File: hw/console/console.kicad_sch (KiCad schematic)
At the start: 147 parts, among them J1 Batt, J301 USB-C 16P, J401 microSD push-push, J501 SPK 8R, J601 FFC-40 0.5mm, Q601 N-MOSFET, SW1 Движок, SW101 UP, SW102 DOWN, SW103 LEFT, SW104 RIGHT, SW105 SELECT, SW106 START, SW107 A, SW108 B, SW109 C, SW110 D, SW2 RESET, SW301 FEL, U1 F133-A, U2 SY8089AAAC, U3 SY8089AAAC, U4 SY8089AAAC, U401 W25Q32JVSSIQ, U5 TP4056, U501 PAM8301, Y1 24 МГц, Y2 32.768 кГц

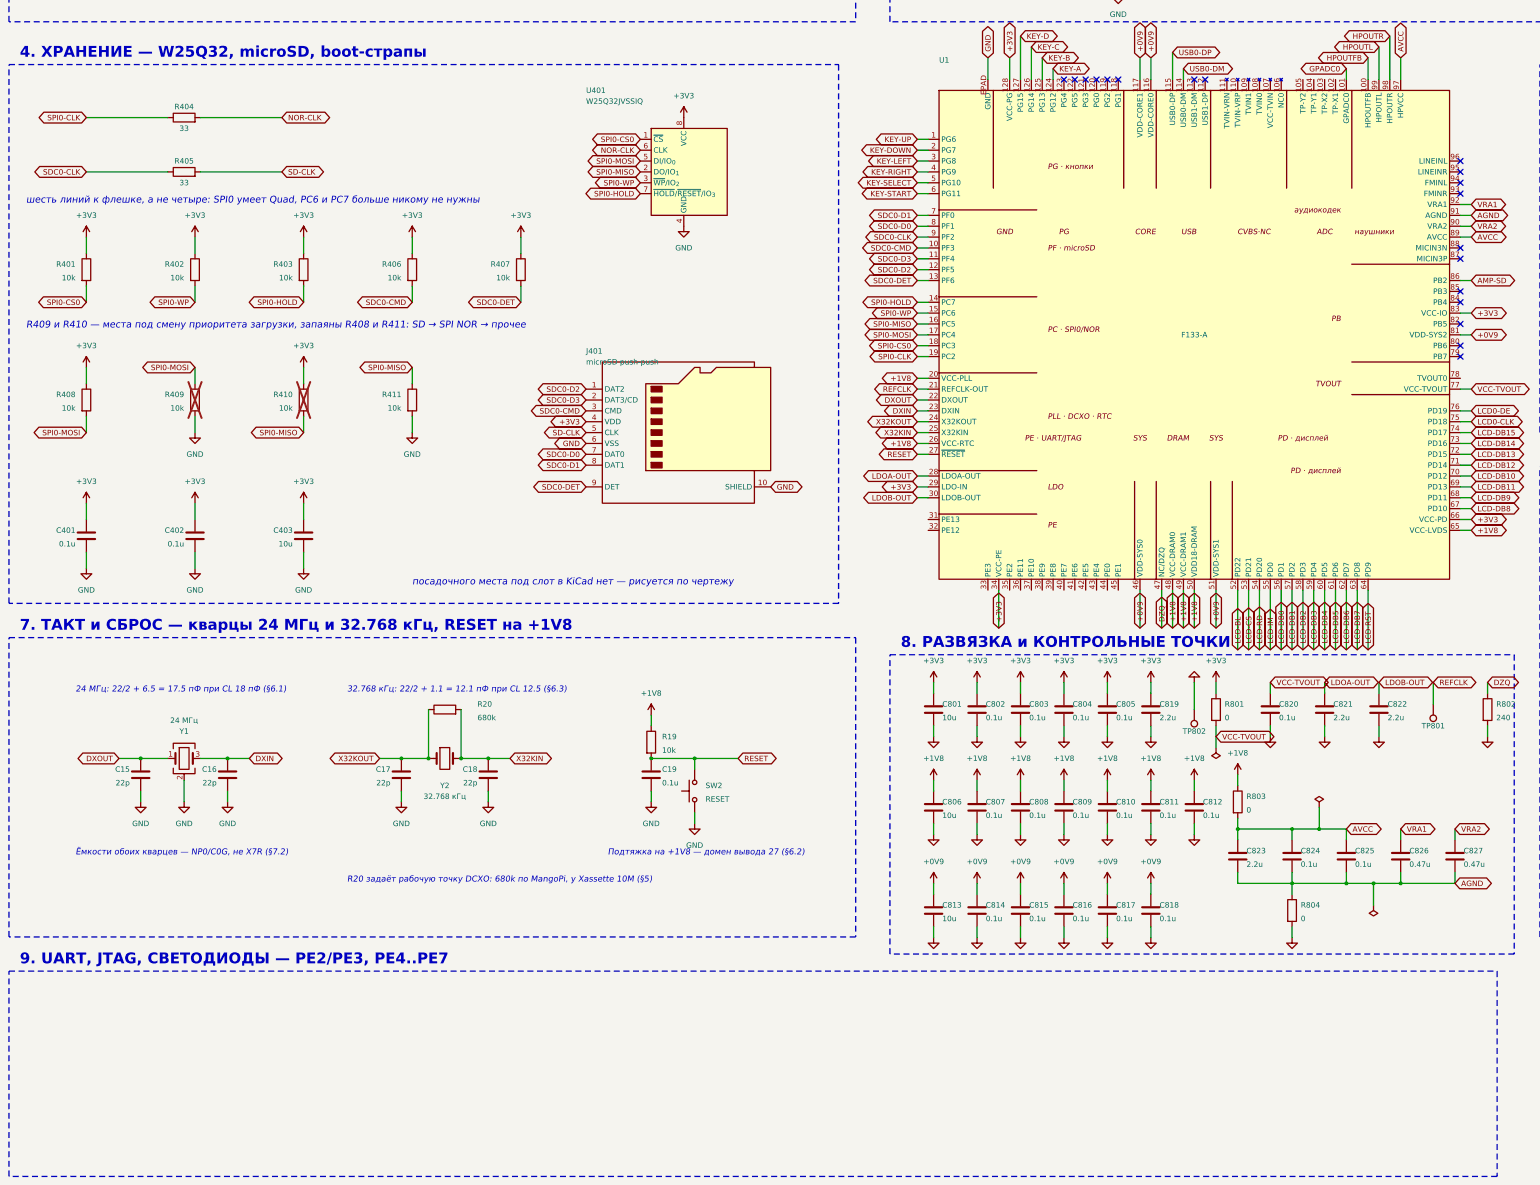
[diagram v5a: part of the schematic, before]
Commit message: hw: блок 9 «UART, JTAG, светодиод» — документ и чертёж, ERC ноль
Гребёнка UART0 на PE2/PE3, четыре площадки R-JTAG на PE4..PE7 плюс земляная,
светодиод питания от рельсы 3.3 В. Восемь деталей, пять из них — пятачки.

Заодно закрыты выводы, у которых не было своего блока: TVOUT0 и четыре
тачскрина — крестики по решению блока 8 §6.4.

Схема закончена: у каждого из 128 выводов F133 либо цепь, либо крестик,
ERC даёт 0 нарушений, весь лист воспроизводится прогоном девяти скриптов.

Co-Authored-By: Claude Opus 5 <noreply@anthropic.com>
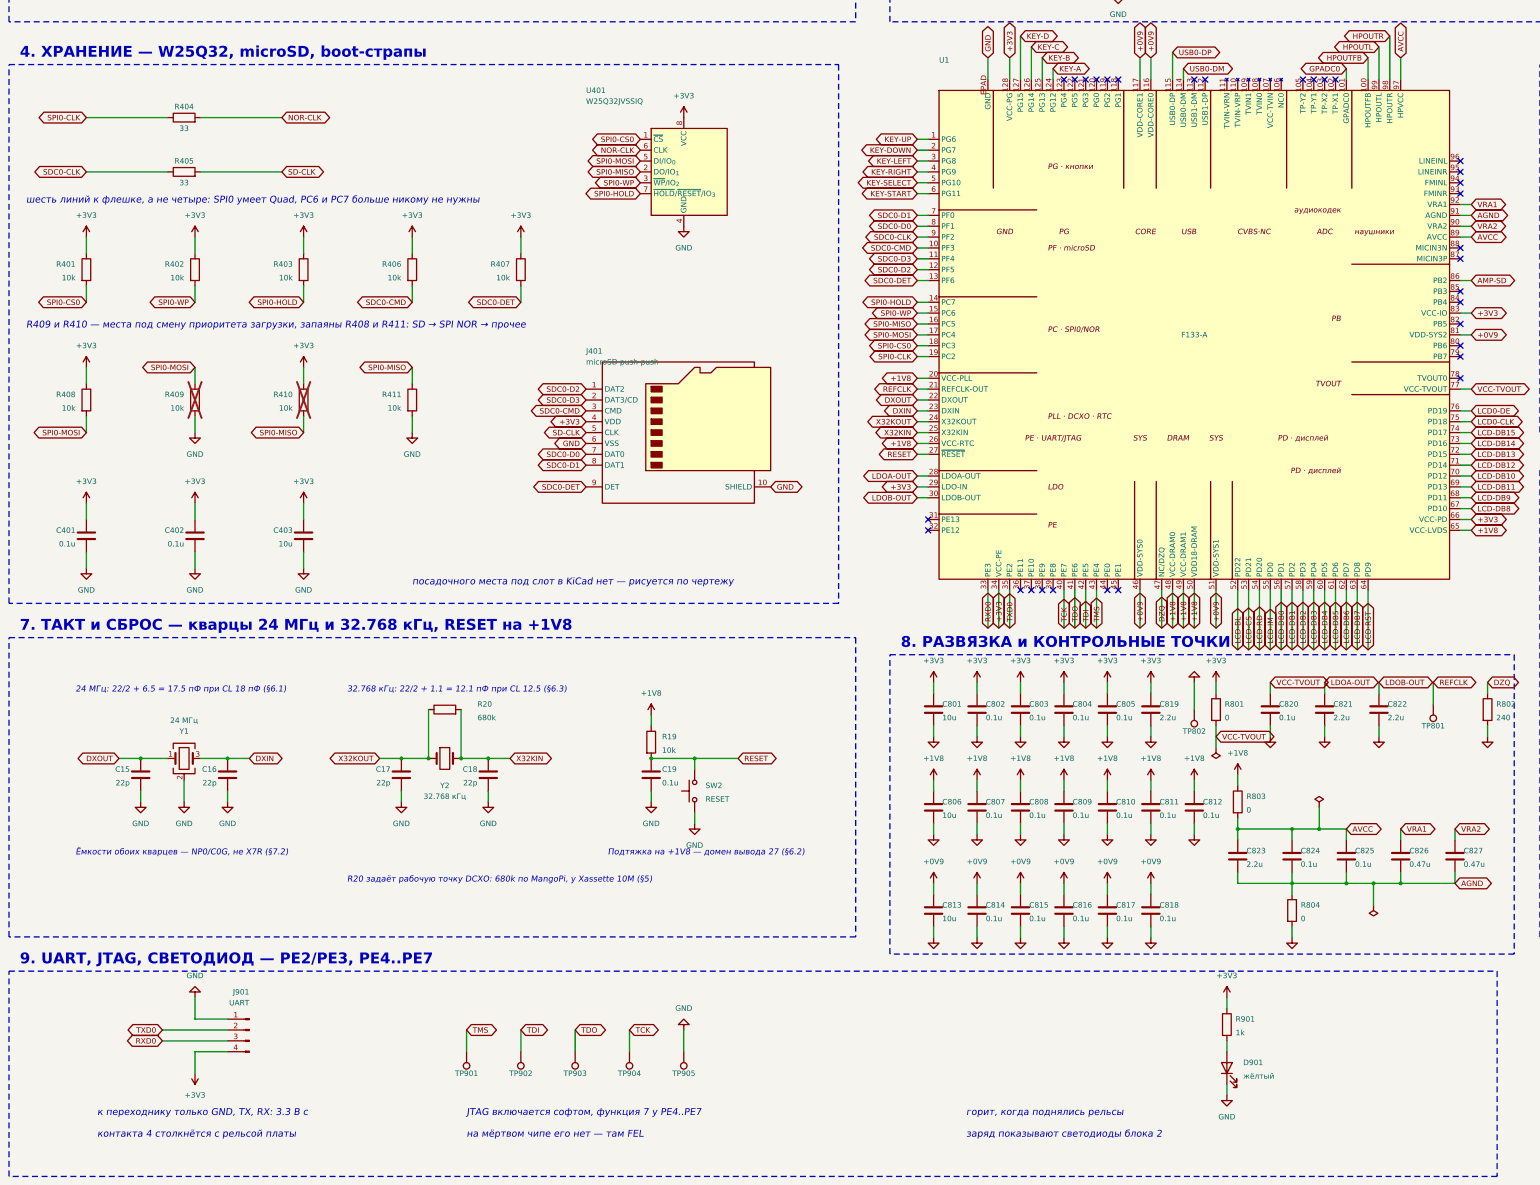
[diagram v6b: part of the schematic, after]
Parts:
- added D901: жёлтый, LED_SMD:LED_0805_2012Metric_Pad1.15x1.40mm_HandSolder, symbol Device:LED
- added J901: UART, Connector_PinHeader_2.54mm:PinHeader_1x04_P2.54mm_Vertical, symbol Connector:Conn_01x04_Pin
- added R901: 1k, Resistor_SMD:R_0805_2012Metric_Pad1.20x1.40mm_HandSolder, symbol Device:R
- added TP901: TMS, TestPoint:TestPoint_Pad_D1.5mm, symbol Connector:TestPoint
- added TP902: TDI, TestPoint:TestPoint_Pad_D1.5mm, symbol Connector:TestPoint
- added TP903: TDO, TestPoint:TestPoint_Pad_D1.5mm, symbol Connector:TestPoint
- added TP904: TCK, TestPoint:TestPoint_Pad_D1.5mm, symbol Connector:TestPoint
- added TP905: GND, TestPoint:TestPoint_Pad_D1.5mm, symbol Connector:TestPoint
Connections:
- net +3V3: now also J901.4 (Pin_4), R901.1
- net GND: now also D901.1 (K), J901.1 (Pin_1), TP905.1
- net RXD0: now reaches U1.33 (PE3)
- net RXD0: now also J901.3 (Pin_3)
- net TXD0: now reaches U1.35 (PE2)
- net TXD0: now also J901.2 (Pin_2)
- net TCK: now reaches U1.40 (PE7)
- net TCK: now also TP904.1
- net TDO: now reaches U1.41 (PE6)
- net TDO: now also TP903.1
- net TDI: now reaches U1.42 (PE5)
- net TDI: now also TP902.1
- net TMS: now reaches U1.43 (PE4)
- net TMS: now also TP901.1
- new net: D901.2 (A), R901.2
- no-connect marks 27 -> 40
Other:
- note added: "9. UART, JTAG, СВЕТОДИОД — PE2/PE3, PE4..PE7"
- note added: "JTAG включается софтом, функция 7 у PE4..PE7"
- note added: "горит, когда поднялись рельсы"
- note added: "заряд показывают светодиоды блока 2"
- note added: "к переходнику только GND, TX, RX: 3.3 В с"
- note added: "контакта 4 столкнётся с рельсой платы"
- note added: "на мёртвом чипе его нет — там FEL"
- note removed: "9. UART, JTAG, СВЕТОДИОДЫ — PE2/PE3, PE4..PE7"

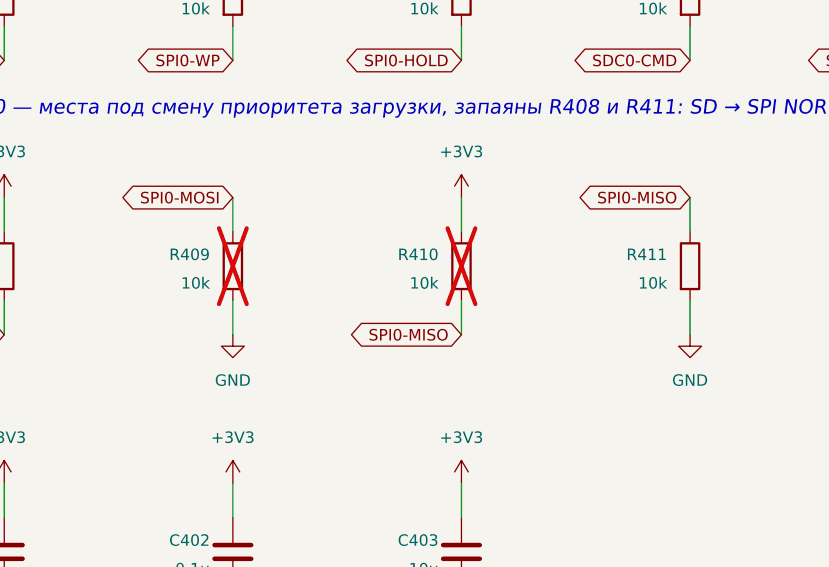
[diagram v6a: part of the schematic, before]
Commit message: hw: страп BOOT-SEL1 не читался нулём — 10k вниз против внутренней подтяжки
У PC3/PC4/PC5 внутренняя подтяжка вверх включена сразу после сброса: Table 4-2
даёт «Reset State PU», регистр PC_PULL0 — значение по умолчанию 0x0000_0540.
Сопротивление известно, Table 5-4: 12/15/18 кОм, впятеро жёстче обычных GPIO.

С резистором 10k вниз PC5 садился на 3.3 x 10/(10+15) = 1.32 В при пороге VIL
0.99 В. То есть BOOT-SEL1 читался бы не нулём, а неопределённым уровнем, и
приоритет загрузки зависел бы от экземпляра чипа.

R409 и R411 -> 2.2k: отношение 2.2/(2.2+12) = 0.155 против предела 0.3, запас
вдвое даже при худшей внутренней подтяжке.

В 04-storage.md §7.2 было прямо написано, что сопротивление внутренней подтяжки
даташит не указывает. Это неверно, и на этом держался выбор 10k.

Заодно у U1 появилось поле Источник — единственная деталь листа без него.

Co-Authored-By: Claude Opus 5 <noreply@anthropic.com>
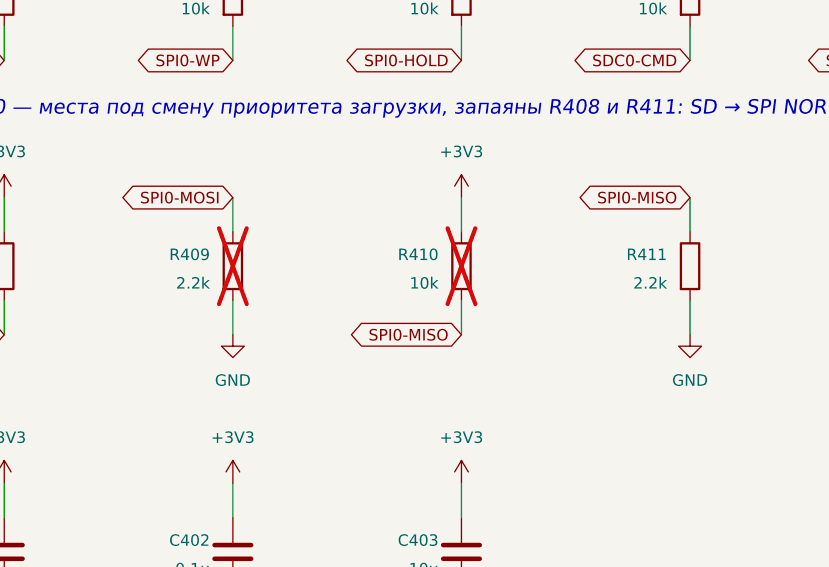
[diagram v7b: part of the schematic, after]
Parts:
- R409, R411: value 10k -> 2.2k
- U1: Источник (none) -> CHIPS.md §1; распиновка — Table 4-2
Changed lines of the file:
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@@
 			)
 		)
+		(property "Источник" "CHIPS.md §1; распиновка — Table 4-2"
+			(at 297.18 203.2 0)
+			(effects
+				(font (size 1.27 1.27))
+				(hide yes)
+			)
+		)
 		(pin "1"
 		)
@@
 			)
 		)
-		(property "Value" "10k"
+		(property "Value" "2.2k"
 			(at 60.96 220.345 0)
 			(effects
@@
 			)
 		)
-		(property "Value" "10k"
+		(property "Value" "2.2k"
 			(at 111.76 220.345 0)
 			(effects
